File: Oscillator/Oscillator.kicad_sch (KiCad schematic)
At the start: 24 parts, among them Q1 NPN, Q2 PNP, U1 40106, U2 TL074, U3 TL074

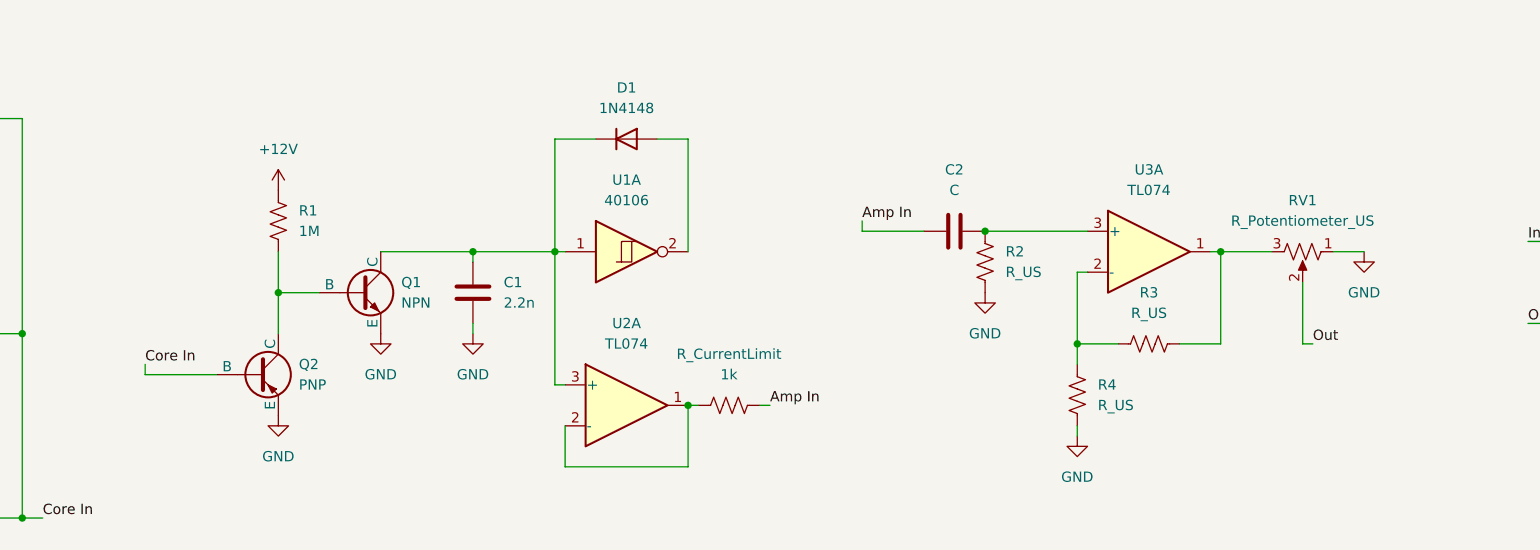
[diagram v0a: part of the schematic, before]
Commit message: added resistor values to the osc.'s amp. cct.
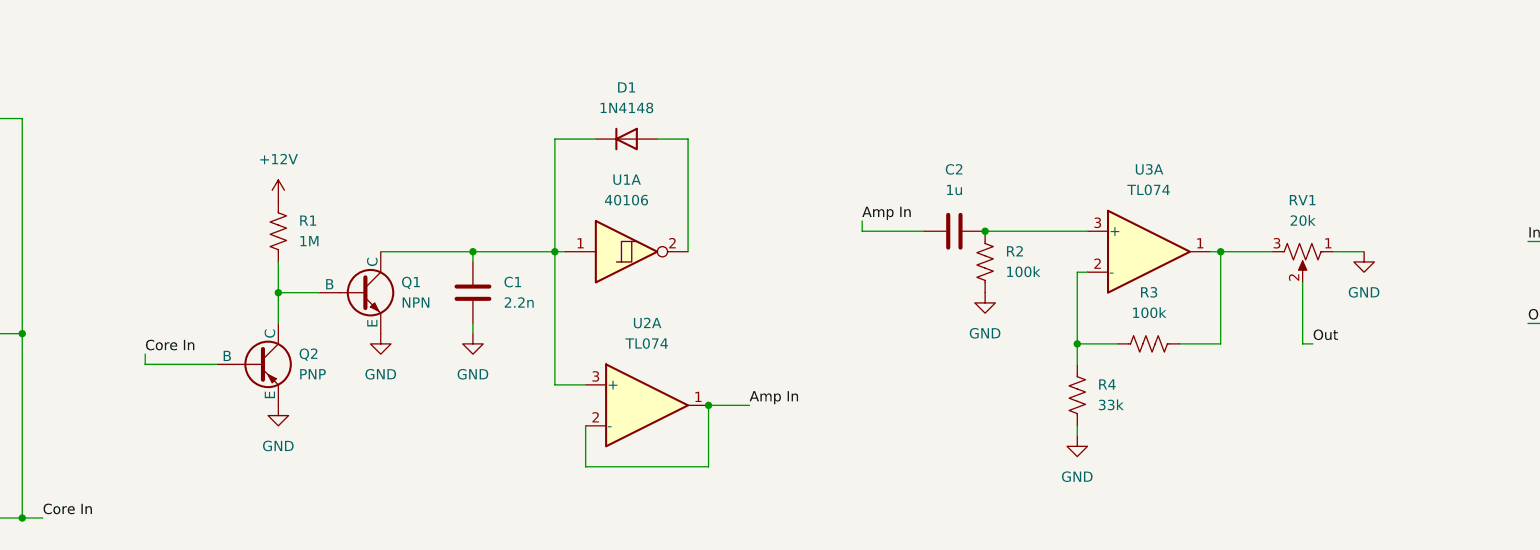
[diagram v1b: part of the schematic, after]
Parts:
- removed R_CurrentLimit: 1k, symbol Device:R_US
- C2: value C -> 1u
- R2, R3: value R_US -> 100k
- R4: value R_US -> 33k
- RV1: value R_Potentiometer_US -> 20k
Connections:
- net Amp In: now also U2.1, U2.2 (-)
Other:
- moved on the sheet: Q2, R1, U2A

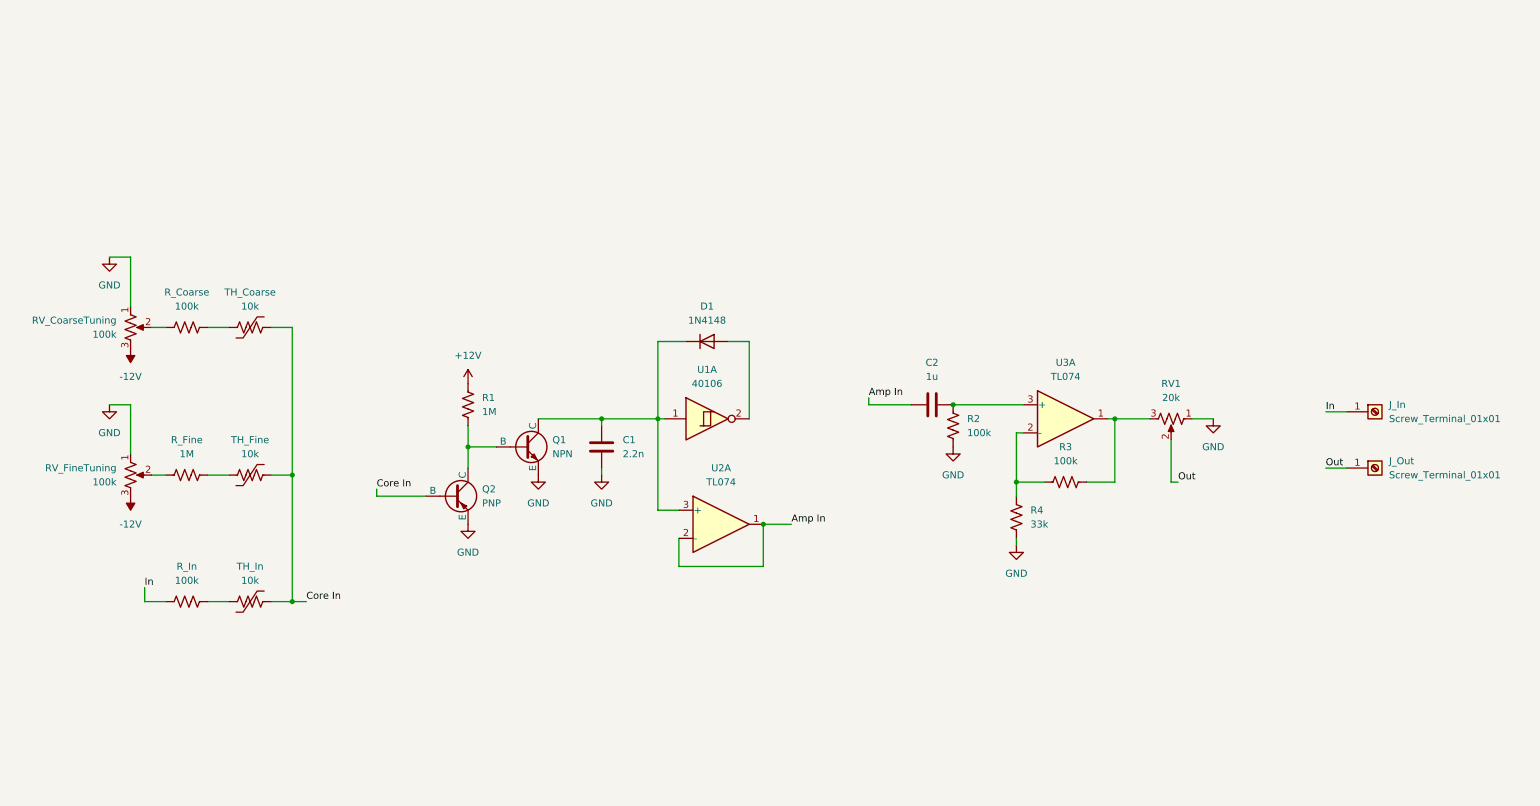
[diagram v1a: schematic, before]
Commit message: added mixer into circuit
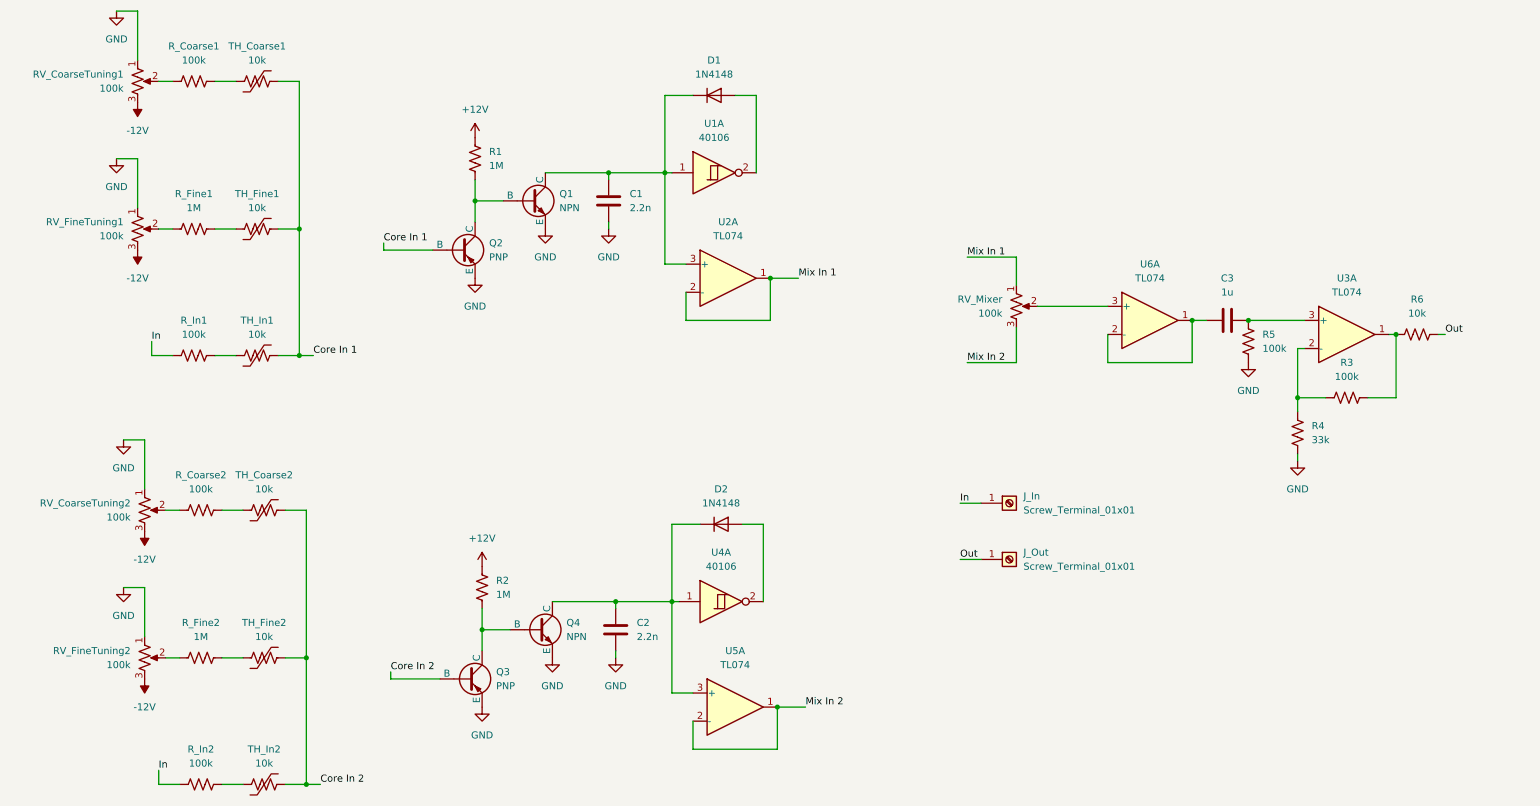
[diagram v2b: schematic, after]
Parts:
- removed RV1: 20k, symbol Device:R_Potentiometer_US
- added C2: 2.2n, symbol Device:C
- added D2: 1N4148, Diode_THT:D_DO-35_SOD27_P7.62mm_Horizontal, symbol Diode:1N4148
- added Q3: PNP, symbol Simulation_SPICE:PNP
- added Q4: NPN, symbol Simulation_SPICE:NPN
- added R2, R_Fine2: 1M, symbol Device:R_US
- added R6: 10k, symbol Device:R_US
- added RV_CoarseTuning2, RV_FineTuning2, RV_Mixer: 100k, symbol Device:R_Potentiometer_US
- added R_Coarse2, R_In2: 100k, symbol Device:R_US
- added TH_Coarse2, TH_Fine2, TH_In2: 10k, symbol Device:Thermistor_US
- added U4: 40106, symbol 4xxx:40106
- added U5, U6: TL074, symbol Amplifier_Operational:TL074
- renumbered C2 to C3, R2 to R5, RV_CoarseTuning to RV_CoarseTuning1, RV_FineTuning to RV_FineTuning1, R_Coarse to R_Coarse1, R_Fine to R_Fine1, R_In to R_In1, TH_Coarse to TH_Coarse1, TH_Fine to TH_Fine1, TH_In to TH_In1
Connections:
- net +12V: now also R2.1
- net -12V: now also RV_CoarseTuning2.3, RV_FineTuning2.3
- net GND: now also C2.2, Q3.3 (E), Q4.3 (E), RV_CoarseTuning2.1, RV_FineTuning2.1
- net In: now also R_In2.1
- net Out: now also R6.2
- net at R3.2, U3.1: now also R6.1
- net Amp In renamed Mix In 1
- net Mix In 1: now also RV_Mixer.1; no longer C3.1
- net Core In renamed Core In 1
- new net: Q3.1 (C), Q4.2 (B), R2.2
- new net: C3.1, U6.1, U6.2 (-)
- new net: RV_Mixer.2, U6.3 (+)
- new net: C2.1, D2.1 (K), Q4.1 (C), U4.1, U5.3 (+)
- new net: D2.2 (A), U4.2
- new net: R_Coarse2.2, TH_Coarse2.1
- new net: R_In2.2, TH_In2.1
- new net: RV_FineTuning2.2, R_Fine2.1
- new net: R_Fine2.2, TH_Fine2.1
- new net: RV_CoarseTuning2.2, R_Coarse2.1
- new net Core In 2: Q3.2 (B), TH_Coarse2.2, TH_Fine2.2, TH_In2.2
- new net Mix In 2: RV_Mixer.3, U5.1, U5.2 (-)
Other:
- moved on the sheet: C1, C3, D1, J_In, J_Out, Q1, Q2, R1, R3, R4, R5, RV_CoarseTuning1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

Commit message: removed unnecessary buffers in front of each osc.
Also put LTspice simulation files in their own folder
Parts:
- removed U2, U5: TL074, symbol Amplifier_Operational:TL074
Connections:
- net Mix In 1: now also C1.1, D1.1 (K), Q1.1 (C), U1.1
- net Mix In 2: now also C2.1, D2.1 (K), Q4.1 (C), U4.1
